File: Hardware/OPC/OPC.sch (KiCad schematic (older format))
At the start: 6 parts

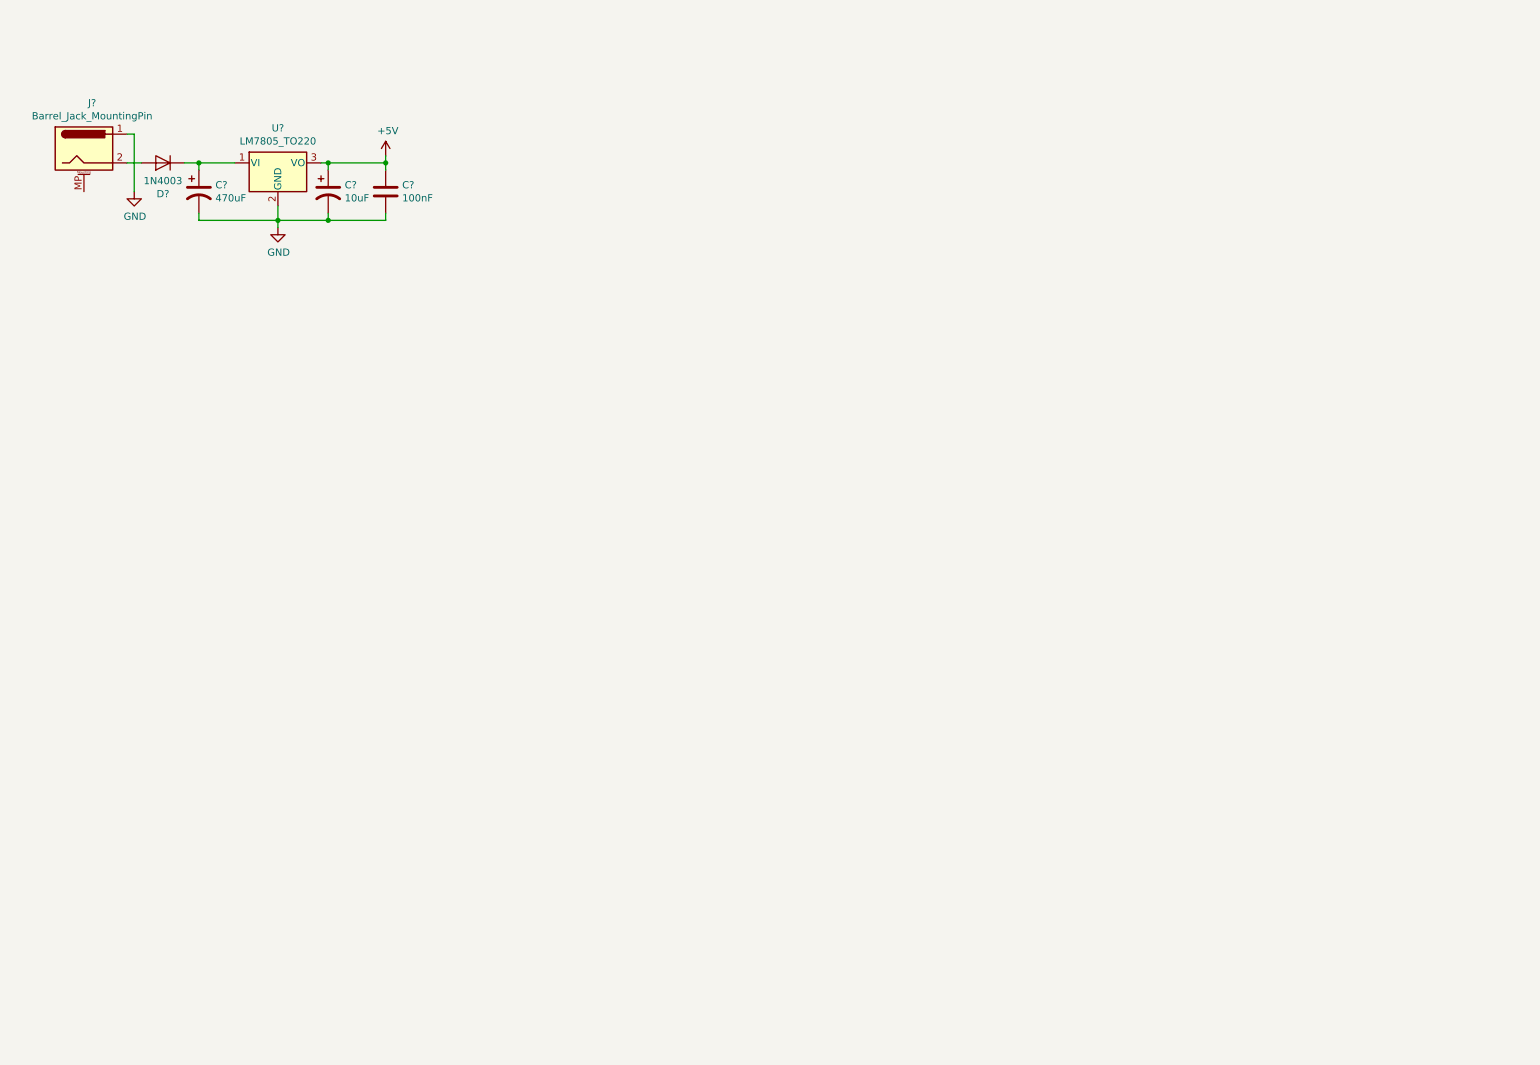
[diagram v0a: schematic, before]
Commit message: Relays added
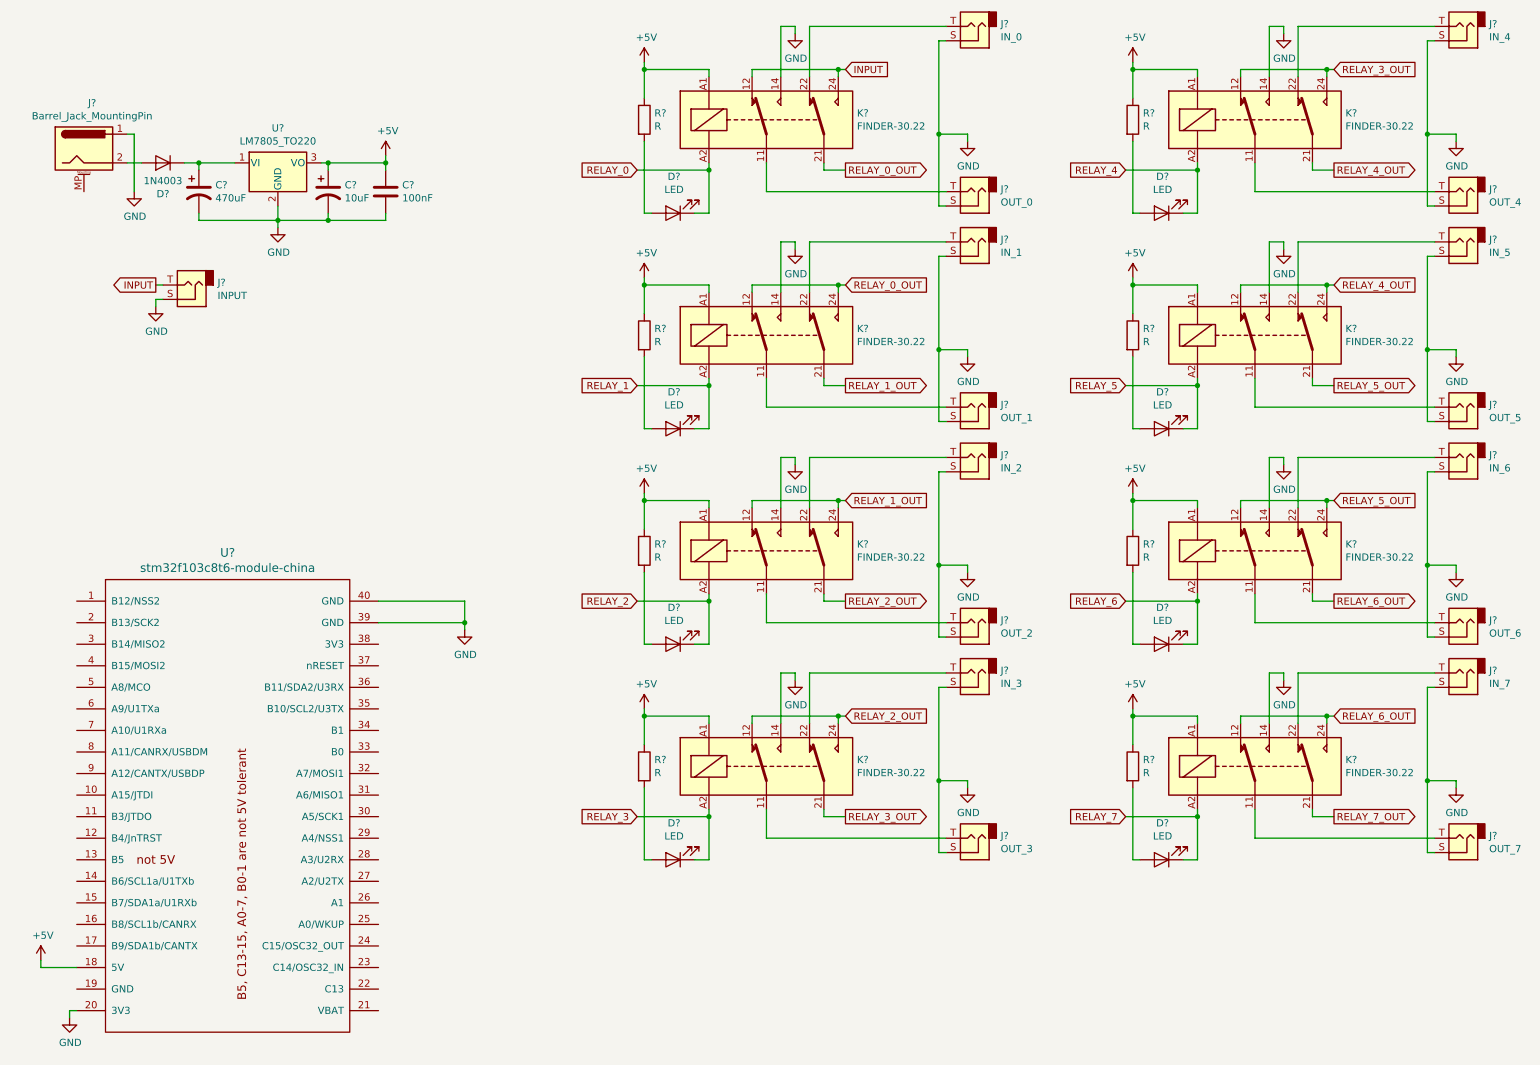
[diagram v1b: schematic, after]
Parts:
- added D? (x8): LED, symbol Device:LED
- added J?: INPUT, symbol Connector:AudioJack2
- added J?: OUT_4, symbol Connector:AudioJack2
- added J?: IN_4, symbol Connector:AudioJack2
- added J?: OUT_5, symbol Connector:AudioJack2
- added J?: IN_5, symbol Connector:AudioJack2
- added J?: OUT_6, symbol Connector:AudioJack2
- added J?: IN_6, symbol Connector:AudioJack2
- added J?: OUT_7, symbol Connector:AudioJack2
- added J?: IN_7, symbol Connector:AudioJack2
- added J?: OUT_0, symbol Connector:AudioJack2
- added J?: IN_0, symbol Connector:AudioJack2
- added J?: OUT_1, symbol Connector:AudioJack2
- added J?: IN_1, symbol Connector:AudioJack2
- added J?: OUT_2, symbol Connector:AudioJack2
- added J?: IN_2, symbol Connector:AudioJack2
- added J?: OUT_3, symbol Connector:AudioJack2
- added J?: IN_3, symbol Connector:AudioJack2
- added K? (x8): FINDER-30.22, Relay_THT:Relay_DPDT_Finder_30.22, symbol Relay:FINDER-30.22
- added R? (x8): R, symbol Device:R
- added U?: stm32f103c8t6-module-china, myelin-kicad:stm32f103c8t6-module-china, symbol STM32F103C8T6_Board:stm32f103c8t6-module-china
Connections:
- net +5V: now also K?.A1, K?.A1, K?.A1, K?.A1, K?.A1, K?.A1, K?.A1, K?.A1, R?.1, R?.1, R?.1, R?.1, R?.1, R?.1, R?.1, R?.1, U?.18 (5V)
- net GND: now also J?.S, J?.S, J?.S, J?.S, J?.S, J?.S, J?.S, J?.S, J?.S, J?.S, J?.S, J?.S, J?.S, J?.S, J?.S, J?.S, J?.S, K?.14, K?.14, K?.14, K?.14, K?.14, K?.14, K?.14, K?.14, U?.20 (3V3), U?.39 (GND), U?.40 (GND)
- new net: J?.T, K?.11 (x8)
- new net: J?.T, K?.22 (x8)
- new net: D?.2 (A), R?.2 (x8)
- new net INPUT: J?.T, K?.12, K?.24
- new net RELAY_0: D?.1 (K), K?.A2
- new net RELAY_0_OUT: K?.12, K?.21, K?.24
- new net RELAY_1: D?.1 (K), K?.A2
- new net RELAY_1_OUT: K?.12, K?.21, K?.24
- new net RELAY_2: D?.1 (K), K?.A2
- new net RELAY_2_OUT: K?.12, K?.21, K?.24
- new net RELAY_3: D?.1 (K), K?.A2
- new net RELAY_3_OUT: K?.12, K?.21, K?.24
- new net RELAY_4: D?.1 (K), K?.A2
- new net RELAY_4_OUT: K?.12, K?.21, K?.24
- new net RELAY_5: D?.1 (K), K?.A2
- new net RELAY_5_OUT: K?.12, K?.21, K?.24
- new net RELAY_6: D?.1 (K), K?.A2
- new net RELAY_6_OUT: K?.12, K?.21, K?.24
- new net RELAY_7: D?.1 (K), K?.A2
- new net RELAY_7_OUT: K?.21

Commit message: Boards separated in sheets
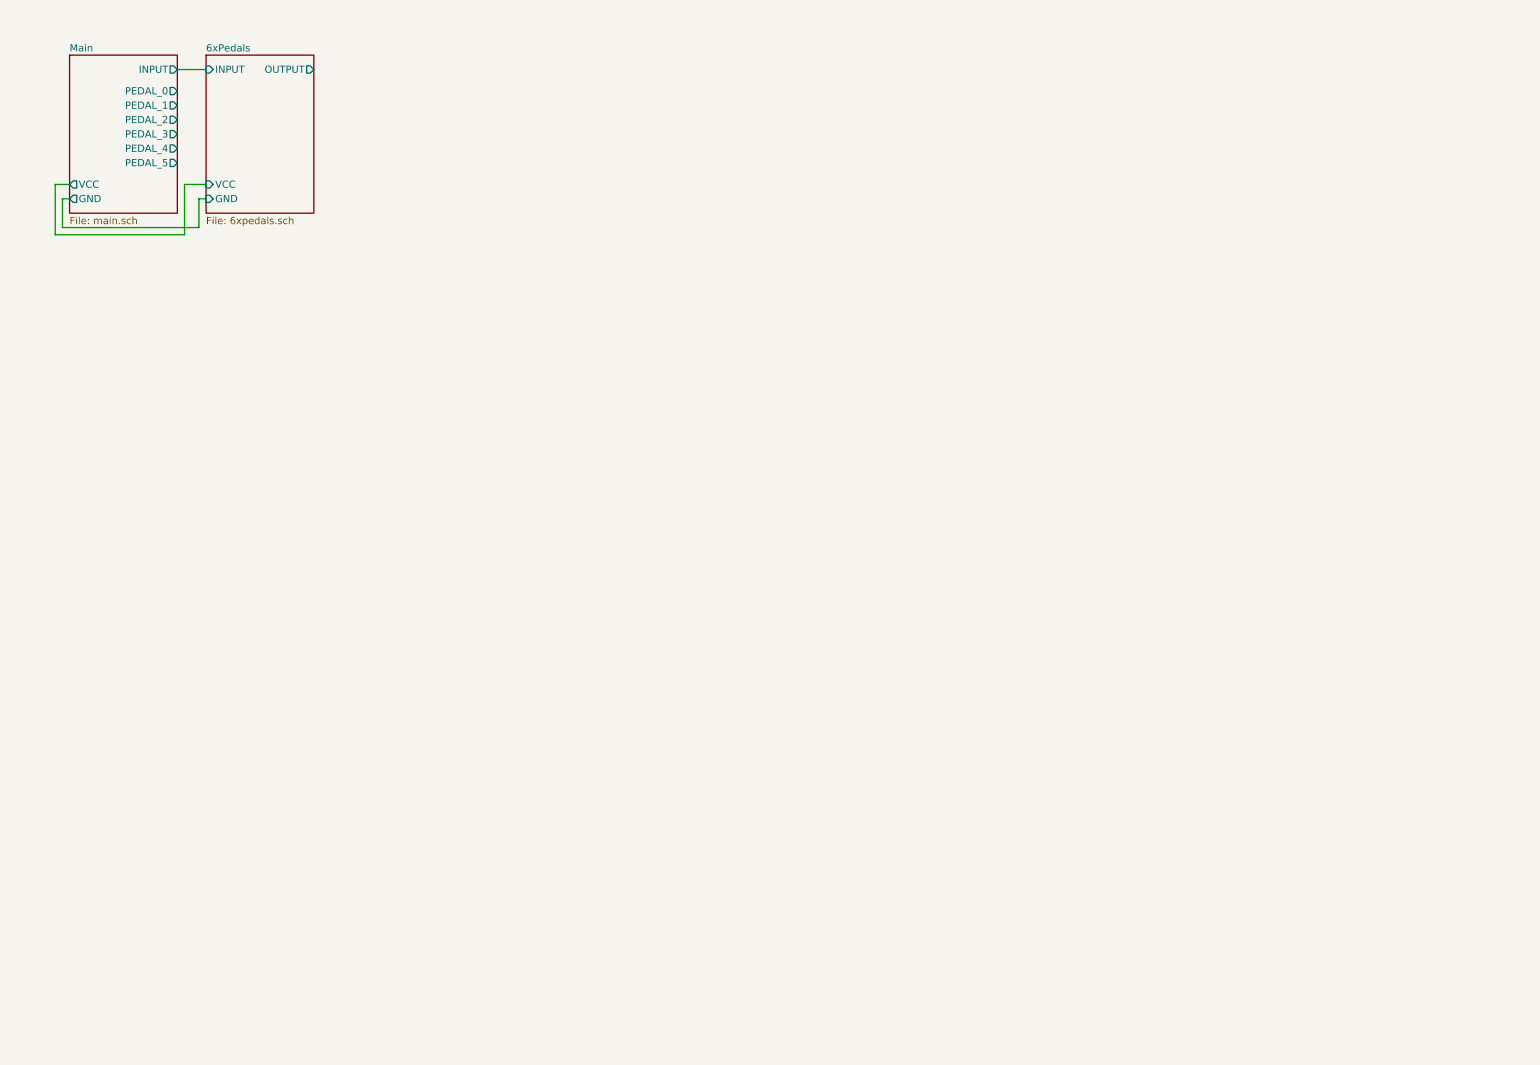
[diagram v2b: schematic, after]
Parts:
- removed C?: 100nF, symbol Device:C
- removed C?: 470uF, symbol Device:CP1
- removed C?: 10uF, symbol Device:CP1
- removed D?: 1N4003, Diode_THT:D_DO-41_SOD81_P10.16mm_Horizontal, symbol Diode:1N4003
- removed D? (x8): LED, symbol Device:LED
- removed J?: Barrel_Jack_MountingPin, symbol Connector:Barrel_Jack_MountingPin
- removed J?: INPUT, symbol Connector:AudioJack2
- removed J?: OUT_4, symbol Connector:AudioJack2
- removed J?: IN_4, symbol Connector:AudioJack2
- removed J?: OUT_5, symbol Connector:AudioJack2
- removed J?: IN_5, symbol Connector:AudioJack2
- removed J?: OUT_6, symbol Connector:AudioJack2
- removed J?: IN_6, symbol Connector:AudioJack2
- removed J?: OUT_7, symbol Connector:AudioJack2
- removed J?: IN_7, symbol Connector:AudioJack2
- removed J?: OUT_0, symbol Connector:AudioJack2
- removed J?: IN_0, symbol Connector:AudioJack2
- removed J?: OUT_1, symbol Connector:AudioJack2
- removed J?: IN_1, symbol Connector:AudioJack2
- removed J?: OUT_2, symbol Connector:AudioJack2
- removed J?: IN_2, symbol Connector:AudioJack2
- removed J?: OUT_3, symbol Connector:AudioJack2
- removed J?: IN_3, symbol Connector:AudioJack2
- removed K? (x8): FINDER-30.22, Relay_THT:Relay_DPDT_Finder_30.22, symbol Relay:FINDER-30.22
- removed R? (x8): R, symbol Device:R
- removed U?: LM7805_TO220, Package_TO_SOT_THT:TO-220-3_Vertical, symbol Regulator_Linear:LM7805_TO220
- removed U?: stm32f103c8t6-module-china, myelin-kicad:stm32f103c8t6-module-china, symbol STM32F103C8T6_Board:stm32f103c8t6-module-china

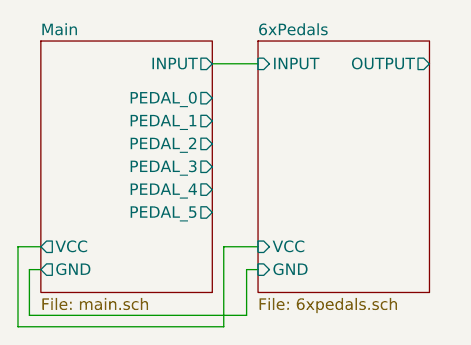
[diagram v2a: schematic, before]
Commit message: Added relay driver
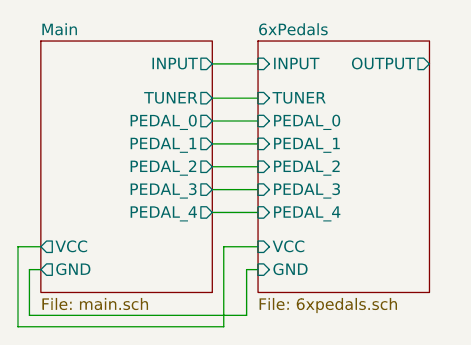
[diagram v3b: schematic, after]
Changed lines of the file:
@@
 F3 "VCC" O L 900 1700 50
 F4 "GND" O L 900 1800 50
-F5 "PEDAL_0" O R 1650 1050 50
-F6 "PEDAL_1" O R 1650 1150 50
-F7 "PEDAL_2" O R 1650 1250 50
-F8 "PEDAL_3" O R 1650 1350 50
-F9 "PEDAL_4" O R 1650 1450 50
-F10 "PEDAL_5" O R 1650 1550 50
+F5 "PEDAL_0" O R 1650 1150 50
+F6 "PEDAL_1" O R 1650 1250 50
+F7 "PEDAL_2" O R 1650 1350 50
+F8 "PEDAL_3" O R 1650 1450 50
+F9 "PEDAL_4" O R 1650 1550 50
+F10 "TUNER" O R 1650 1050 50
 $EndSheet
 $Sheet
@@
 F4 "INPUT" I L 1850 900 50
 F5 "OUTPUT" O R 2600 900 50
+F6 "TUNER" I L 1850 1050 50
+F7 "PEDAL_0" I L 1850 1150 50
+F8 "PEDAL_1" I L 1850 1250 50
+F9 "PEDAL_2" I L 1850 1350 50
+F10 "PEDAL_3" I L 1850 1450 50
+F11 "PEDAL_4" I L 1850 1550 50
 $EndSheet
 Wire Wire Line
@@
 Wire Wire Line
 	1650 900  1850 900
+Wire Wire Line
+	1650 1550 1850 1550
+Wire Wire Line
+	1850 1450 1650 1450
+Wire Wire Line
+	1650 1350 1850 1350
+Wire Wire Line
+	1850 1250 1650 1250
+Wire Wire Line
+	1650 1150 1850 1150
+Wire Wire Line
+	1850 1050 1650 1050
 $EndSCHEMATC

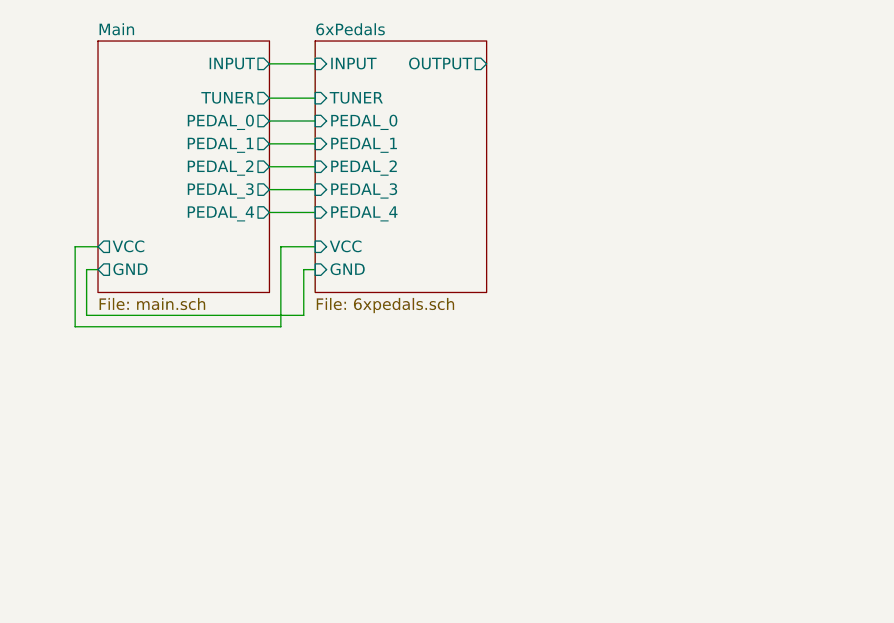
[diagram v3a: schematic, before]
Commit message: Added 7 seg display
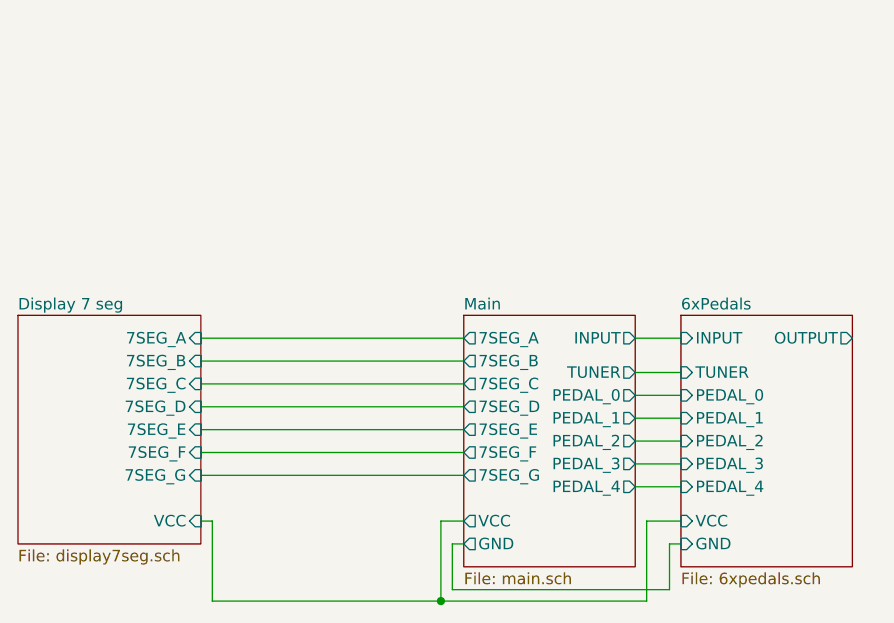
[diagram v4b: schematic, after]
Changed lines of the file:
@@
 $Descr A4 11693 8268
 encoding utf-8
-Sheet 1 3
+Sheet 1 4
 Title ""
 Date ""
@@
 $EndDescr
 $Sheet
-S 900  800  750  1100
+S 2500 2000 750  1100
 U 5E59EF44
 F0 "Main" 50
 F1 "main.sch" 50
-F2 "INPUT" O R 1650 900 50
-F3 "VCC" O L 900 1700 50
-F4 "GND" O L 900 1800 50
-F5 "PEDAL_0" O R 1650 1150 50
-F6 "PEDAL_1" O R 1650 1250 50
-F7 "PEDAL_2" O R 1650 1350 50
-F8 "PEDAL_3" O R 1650 1450 50
-F9 "PEDAL_4" O R 1650 1550 50
-F10 "TUNER" O R 1650 1050 50
+F2 "INPUT" O R 3250 2100 50
+F3 "VCC" O L 2500 2900 50
+F4 "GND" O L 2500 3000 50
+F5 "PEDAL_0" O R 3250 2350 50
+F6 "PEDAL_1" O R 3250 2450 50
+F7 "PEDAL_2" O R 3250 2550 50
+F8 "PEDAL_3" O R 3250 2650 50
+F9 "PEDAL_4" O R 3250 2750 50
+F10 "TUNER" O R 3250 2250 50
+F11 "7SEG_A" O L 2500 2100 50
+F12 "7SEG_B" O L 2500 2200 50
+F13 "7SEG_C" O L 2500 2300 50
+F14 "7SEG_D" O L 2500 2400 50
+F15 "7SEG_F" O L 2500 2600 50
+F16 "7SEG_G" O L 2500 2700 50
+F17 "7SEG_E" O L 2500 2500 50
 $EndSheet
 $Sheet
-S 1850 800  750  1100
+S 3450 2000 750  1100
 U 5E65E563
 F0 "6xPedals" 50
 F1 "6xpedals.sch" 50
-F2 "VCC" I L 1850 1700 50
-F3 "GND" I L 1850 1800 50
-F4 "INPUT" I L 1850 900 50
-F5 "OUTPUT" O R 2600 900 50
-F6 "TUNER" I L 1850 1050 50
-F7 "PEDAL_0" I L 1850 1150 50
-F8 "PEDAL_1" I L 1850 1250 50
-F9 "PEDAL_2" I L 1850 1350 50
-F10 "PEDAL_3" I L 1850 1450 50
-F11 "PEDAL_4" I L 1850 1550 50
+F2 "VCC" I L 3450 2900 50
+F3 "GND" I L 3450 3000 50
+F4 "INPUT" I L 3450 2100 50
+F5 "OUTPUT" O R 4200 2100 50
+F6 "TUNER" I L 3450 2250 50
+F7 "PEDAL_0" I L 3450 2350 50
+F8 "PEDAL_1" I L 3450 2450 50
+F9 "PEDAL_2" I L 3450 2550 50
+F10 "PEDAL_3" I L 3450 2650 50
+F11 "PEDAL_4" I L 3450 2750 50
 $EndSheet
 Wire Wire Line
-	900  1800 850  1800
+	2500 3000 2450 3000
 Wire Wire Line
-	850  1800 850  2000
+	2450 3000 2450 3200
 Wire Wire Line
-	850  2000 1800 2000
+	2450 3200 3400 3200
 Wire Wire Line
-	1800 2000 1800 1800
+	3400 3200 3400 3000
 Wire Wire Line
-	1800 1800 1850 1800
+	3400 3000 3450 3000
 Wire Wire Line
-	900  1700 800  1700
+	2500 2900 2400 2900
 Wire Wire Line
-	800  1700 800  2050
+	2400 2900 2400 3250
 Wire Wire Line
-	800  2050 1700 2050
+	2400 3250 3300 3250
 Wire Wire Line
-	1700 2050 1700 1700
+	3300 3250 3300 2900
 Wire Wire Line
-	1700 1700 1850 1700
+	3300 2900 3450 2900
 Wire Wire Line
-	1650 900  1850 900
+	3250 2100 3450 2100
 Wire Wire Line
-	1650 1550 1850 1550
+	3250 2750 3450 2750
 Wire Wire Line
-	1850 1450 1650 1450
+	3450 2650 3250 2650
 Wire Wire Line
-	1650 1350 1850 1350
+	3250 2550 3450 2550
 Wire Wire Line
-	1850 1250 1650 1250
+	3450 2450 3250 2450
 Wire Wire Line
-	1650 1150 1850 1150
+	3250 2350 3450 2350
 Wire Wire Line
-	1850 1050 1650 1050
+	3450 2250 3250 2250
+$Sheet
+S 550  2000 800  1000
+U 5E472FEB
+F0 "Display 7 seg" 50
+F1 "display7seg.sch" 50
+F2 "7SEG_A" I R 1350 2100 50
+F3 "7SEG_B" I R 1350 2200 50
+F4 "7SEG_C" I R 1350 2300 50
+F5 "7SEG_D" I R 1350 2400 50
+F6 "7SEG_E" I R 1350 2500 50
+F7 "7SEG_F" I R 1350 2600 50
+F8 "7SEG_G" I R 1350 2700 50
+F9 "VCC" I R 1350 2900 50
+$EndSheet
+Wire Wire Line
+	1350 2900 1400 2900
+Wire Wire Line
+	1400 2900 1400 3250
+Wire Wire Line
+	1400 3250 2400 3250
+Connection ~ 2400 3250
+Wire Wire Line
+	1350 2100 2500 2100
+Wire Wire Line
+	2500 2200 1350 2200
+Wire Wire Line
+	1350 2300 2500 2300
+Wire Wire Line
+	2500 2400 1350 2400
+Wire Wire Line
+	1350 2500 2500 2500
+Wire Wire Line
+	2500 2600 1350 2600
+Wire Wire Line
+	1350 2700 2500 2700
 $EndSCHEMATC
